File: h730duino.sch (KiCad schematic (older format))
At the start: 71 parts, among them J4 105162-0001, P1 Digital, P10 CONN_01X01, P11 CONN_01X01, P13 CONN_01X01, P2 Power, P3 Analog, P4 Analog, P5 PWM, P6 PWM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

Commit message: Replace non stocked components.
 - Redesign 5V/3.3V using TPS6216xDSGT
 - Use bigger crystal (move to 5031 case)
 - Change some components parts

Signed-off-by: Martin Ribelotta <martinribelotta@gmail.com>
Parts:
- removed C18, C22: 100n, Capacitor_SMD:C_0603_1608Metric, symbol Device:C_Small
- removed C20, C24: 2.2u, Capacitor_SMD:C_0603_1608Metric, symbol Device:C_Small
- removed U3: AP63203WU, Package_TO_SOT_SMD:TSOT-23-6, symbol Regulator_Switching:AP63203WU
- removed U4: AP63205WU, Package_TO_SOT_SMD:TSOT-23-6, symbol Regulator_Switching:AP63205WU
- added U3: TPS62162DSG, Package_SON:WSON-8-1EP_2x2mm_P0.5mm_EP0.9x1.6mm_ThermalVias, symbol Regulator_Switching:TPS62162DSG
- added U4: TPS62163DSG, Package_SON:WSON-8-1EP_2x2mm_P0.5mm_EP0.9x1.6mm_ThermalVias, symbol Regulator_Switching:TPS62163DSG
- C1: DESCRIPTION (none) -> Capacitor 4.7u 0603
- C10, C12: DESCRIPTION (none) -> Capacitor 20p 0603
- C11, C8, C9: DESCRIPTION (none) -> Capacitor 10p 0603
- C13: DESCRIPTION (none) -> Capacitor 1u 0603
- C14, C15, C16, C2, C3, C39, C4, C40, C41, C43, C44, C45, C46, C47, C48, C5, C6, C7: DESCRIPTION (none) -> Capacitor 100n 0603
- C17, C21: DESCRIPTION (none) -> Capacitor 10u 0603
- C19, C23: value 2.2u -> 22u; DESCRIPTION (none) -> Capacitor 2.2u 0603
- C42: DESCRIPTION (none) -> Capacitor 2.2u 0603
- D3, D4: DESCRIPTION (none) -> Led SMD 0603 red
- L1, L2: DESCRIPTION (none) -> ferrite bead 0603
- L3, L4: value 4.7u -> NR3015T2R2M; footprint Inductor_SMD:L_1210_3225Metric -> Inductor_SMD:L_Taiyo-Yuden_MD-3030; DESCRIPTION (none) -> Inductor 4.7uH 1210
- R26, R4, R5: DESCRIPTION (none) -> Resistor 1.5K 0603
- U1: DESCRIPTION (none) -> STM32H730ZBT6
- U10: DESCRIPTION (none) -> APS6404L-3SQN
- U12: DESCRIPTION (none) -> AP22814BW5
- U2: DESCRIPTION (none) -> W25Q32JVSS
- U5, U6, U8: DESCRIPTION (none) -> MAX40200AUK
- Y1: DESCRIPTION (none) -> Crystal 32.768KHz 3215
- Y2: footprint footprints:Crystal_SMD_3215-2Pin_3.2x1.5mm -> Crystal:Crystal_SMD_5032-2Pin_5.0x3.2mm; DESCRIPTION (none) -> Crystal 8MHz 3215
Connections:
- wire segments 265 -> 267
- no-connect marks 9 -> 11
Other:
- moved on the sheet: C17, C19, C21, C23, D3, D4, L4, R26, R4

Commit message: Fix in design:
 - Add r-series to QSPI interfaces
 - Change vCAP from 100n to 2.2u
 - Add pullup to SWCK/DIO and nRST
 - Remove AGND/DGND separation

Signed-off-by: Martin Ribelotta <martinribelotta@gmail.com>
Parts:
- removed L2: ferrite, Inductor_SMD:L_0603_1608Metric, symbol Device:L_Small
- added R20: 10K, Resistor_SMD:R_0603_1608Metric, symbol Device:R_Small
- added RN1: 0Rx5, Resistor_SMD:R_Array_Convex_5x0603, symbol Device:R_Pack05
- C14, C15: value 100n -> 2.2u
- R5: value 1K5 -> 10K
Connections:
- net labels removed: GNDA
- wire segments 267 -> 269
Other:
- moved on the sheet: SW1
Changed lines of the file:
@@
 L power:GND #PWR017
 U 1 1 602274CF
-P 850 2550
-F 0 "#PWR017" H 850 2300 50  0001 C CNN
-F 1 "GND" V 855 2422 50  0000 R CNN
-F 2 "" H 850 2550 50  0000 C CNN
-F 3 "" H 850 2550 50  0000 C CNN
-	1    850  2550
+P 800 2600
+F 0 "#PWR017" H 800 2350 50  0001 C CNN
+F 1 "GND" V 805 2472 50  0000 R CNN
+F 2 "" H 800 2600 50  0000 C CNN
+F 3 "" H 800 2600 50  0000 C CNN
+	1    800  2600
 	0    1    1    0
 $EndComp
@@
 P 3600 2850
 F 0 "C15" H 3508 2896 50  0000 R CNN
-F 1 "100n" H 3508 2805 50  0000 R CNN
+F 1 "2.2u" H 3508 2805 50  0000 R CNN
 F 2 "Capacitor_SMD:C_0603_1608Metric" H 3600 2850 50  0001 C CNN
 F 3 "~" H 3600 2850 50  0001 C CNN
@@
 P 4000 2850
 F 0 "C14" H 3908 2896 50  0000 R CNN
-F 1 "100n" H 3908 2805 50  0000 R CNN
+F 1 "2.2u" H 3908 2805 50  0000 R CNN
 F 2 "Capacitor_SMD:C_0603_1608Metric" H 4000 2850 50  0001 C CNN
 F 3 "~" H 4000 2850 50  0001 C CNN
@@
 L Switch:SW_Push SW1
 U 1 1 609B261A
-P 1050 2550
-F 0 "SW1" H 1050 2457 50  0000 C CNN
-F 1 "RESET" H 1050 2366 50  0000 C CNN
-F 2 "Button_Switch_THT:SW_Tactile_SPST_Angled_PTS645Vx39-2LFS" H 1050 2750 50  0001 C CNN
-F 3 "~" H 1050 2750 50  0001 C CNN
-	1    1050 2550
+P 1000 2600
+F 0 "SW1" H 1000 2507 50  0000 C CNN
+F 1 "RESET" H 1000 2416 50  0000 C CNN
+F 2 "Button_Switch_THT:SW_Tactile_SPST_Angled_PTS645Vx39-2LFS" H 1000 2800 50  0001 C CNN
+F 3 "~" H 1000 2800 50  0001 C CNN
+	1    1000 2600
 	1    0    0    -1
 $EndComp
@@
 P 850 2100
 F 0 "R5" H 792 2054 50  0000 R CNN
-F 1 "1K5" H 792 2145 50  0000 R CNN
+F 1 "10K" H 792 2145 50  0000 R CNN
 F 2 "Resistor_SMD:R_0603_1608Metric" H 850 2100 50  0001 C CNN
 F 3 "~" H 850 2100 50  0001 C CNN
@@
 	1    0    0    -1
 $EndComp
-Wire Wire Line
-	900  3750 1150 3750
-$Comp
-L Device:L_Small L2
-U 1 1 601A7F71
-P 800 3750
-F 0 "L2" V 711 3750 50  0000 C CNN
-F 1 "ferrite" V 620 3750 50  0000 C CNN
-F 2 "Inductor_SMD:L_0603_1608Metric" H 800 3750 50  0001 C CNN
-F 3 "~" H 800 3750 50  0001 C CNN
-F 4 "ferrite bead 0603" H 800 3750 50  0001 C CNN "DESCRIPTION"
-	1    800  3750
-	0    -1   -1   0
-$EndComp
 Connection ~ 1150 3750
-$Comp
-L power:GNDA #PWR014
-U 1 1 601A26C1
-P 1150 3750
-F 0 "#PWR014" H 1150 3500 50  0001 C CNN
-F 1 "GNDA" H 1155 3577 50  0000 C CNN
-F 2 "" H 1150 3750 50  0001 C CNN
-F 3 "" H 1150 3750 50  0001 C CNN
-	1    1150 3750
-	1    0    0    -1
-$EndComp
 Wire Wire Line
 	1150 3550 900  3550
@@
 Wire Wire Line
 	650  3550 700  3550
-Wire Wire Line
-	700  3750 650  3750
 $Comp
 L power:GND #PWR0110
@@
 Wire Wire Line
 	950  2000 1800 2000
-Text Label 1400 2550 0    50   ~ 0
+Text Label 1250 2600 0    50   ~ 0
 ~RST
-Wire Wire Line
-	1400 2550 1250 2550
 $Comp
 L stm32h730zbtx:STM32H730ZBT6 U1
@@
 Text Label 5300 2150 2    50   ~ 0
 USR_LED
-Text Label 5300 2750 2    50   ~ 0
+Text Label 4750 2750 2    50   ~ 0
 OCTOSPIM_P2_CLK
 Text Label 7700 3800 0    50   ~ 0
@@
 Connection ~ 1500 3550
 Wire Wire Line
-	650  3750 650  3950
-Wire Wire Line
 	650  3550 650  3300
 $Comp
 L power:GND #PWR0113
 U 1 1 60346253
-P 650 3950
-F 0 "#PWR0113" H 650 3700 50  0001 C CNN
-F 1 "GND" H 655 3777 50  0000 C CNN
-F 2 "" H 650 3950 50  0000 C CNN
-F 3 "" H 650 3950 50  0000 C CNN
-	1    650  3950
+P 1150 3750
+F 0 "#PWR0113" H 1150 3500 50  0001 C CNN
+F 1 "GND" H 1155 3577 50  0000 C CNN
+F 2 "" H 1150 3750 50  0000 C CNN
+F 3 "" H 1150 3750 50  0000 C CNN
+	1    1150 3750
 	1    0    0    -1
 $EndComp
@@
 	1    0    0    -1
 $EndComp
-Text Label 5300 2350 2    50   ~ 0
+Text Label 4750 2350 2    50   ~ 0
 OCTOSPIM_P2_IO0
-Text Label 5300 2450 2    50   ~ 0
+Text Label 4750 2450 2    50   ~ 0
 OCTOSPIM_P2_IO1
-Text Label 5300 2550 2    50   ~ 0
+Text Label 4750 2550 2    50   ~ 0
 OCTOSPIM_P2_IO2
-Text Label 5300 2650 2    50   ~ 0
+Text Label 4750 2650 2    50   ~ 0
 OCTOSPIM_P2_IO3
 Text Label 10400 6600 0    50   ~ 0
@@
 	10950 2200 10850 2200
 Connection ~ 10850 2200
+$Comp
+L Device:R_Small R20
+U 1 1 605BF408
+P 1500 2600
+F 0 "R20" V 1304 2600 50  0000 C CNN
+F 1 "10K" V 1395 2600 50  0000 C CNN
+F 2 "Resistor_SMD:R_0603_1608Metric" H 1500 2600 50  0001 C CNN
+F 3 "~" H 1500 2600 50  0001 C CNN
+F 4 "Resistor 1.5K 0603" H 1500 2600 50  0001 C CNN "DESCRIPTION"
+	1    1500 2600
+	0    -1   1    0
+$EndComp
+$Comp
+L power:+3V3 #PWR014
+U 1 1 605C04C4
+P 1600 2600
+F 0 "#PWR014" H 1600 2450 50  0001 C CNN
+F 1 "+3.3V" V 1615 2728 50  0000 L CNN
+F 2 "" H 1600 2600 50  0000 C CNN
+F 3 "" H 1600 2600 50  0000 C CNN
+	1    1600 2600
+	0    1    1    0
+$EndComp
+Wire Wire Line
+	1200 2600 1400 2600
+$Comp
+L Device:R_Pack05 RN1
+U 1 1 60649F7B
+P 4950 2550
+F 0 "RN1" V 5283 2550 50  0000 C CNN
+F 1 "0Rx5" V 5374 2550 50  0000 C CNN
+F 2 "Resistor_SMD:R_Array_Convex_5x0603" V 5325 2550 50  0001 C CNN
+F 3 "~" H 4950 2550 50  0001 C CNN
+	1    4950 2550
+	0    1    1    0
+$EndComp
+Wire Wire Line
+	5150 2350 5300 2350
+Wire Wire Line
+	5300 2450 5150 2450
+Wire Wire Line
+	5150 2550 5300 2550
+Wire Wire Line
+	5300 2650 5150 2650
+Wire Wire Line
+	5150 2750 5300 2750
 $EndSCHEMATC

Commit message: Major rework:
 - Split flash/ram in two QSPI iface
   - Flash is connected to QSPI2
   - PSRAM is connected to QSPI1
 - Move QSPI PSRAM near to P1
 - Reorder pins to P1 and P5
 - Reasign I2C5, UART4 to more convenient place
 - Reasign PWM pins to more convenient place
 - Rerarrange 25MHz ETHPHY crystal

Signed-off-by: Martin Ribelotta <martinribelotta@gmail.com>
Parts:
- removed P9: EXT, Socket_Arduino_Mega:Socket_Strip_Arduino_1x10, symbol Connector_Generic:Conn_01x10
- removed RN1: 0Rx5, Resistor_SMD:R_Array_Convex_5x0603, symbol Device:R_Pack05
- added J7: Conn_02x03_Odd_Even, Connector_PinHeader_2.54mm:PinHeader_2x03_P2.54mm_Vertical, symbol Connector_Generic:Conn_02x03_Odd_Even
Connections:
- net labels added: OCTOSPIM_P1_CLK, OCTOSPIM_P1_IO4, OCTOSPIM_P1_IO5, OCTOSPIM_P1_IO6, OCTOSPIM_P1_IO7
- net labels removed: EXT5, EXT6, EXT7, EXT8, EXT9
- wire segments 269 -> 267
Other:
- moved on the sheet: C41, D3, D4, R26, R4

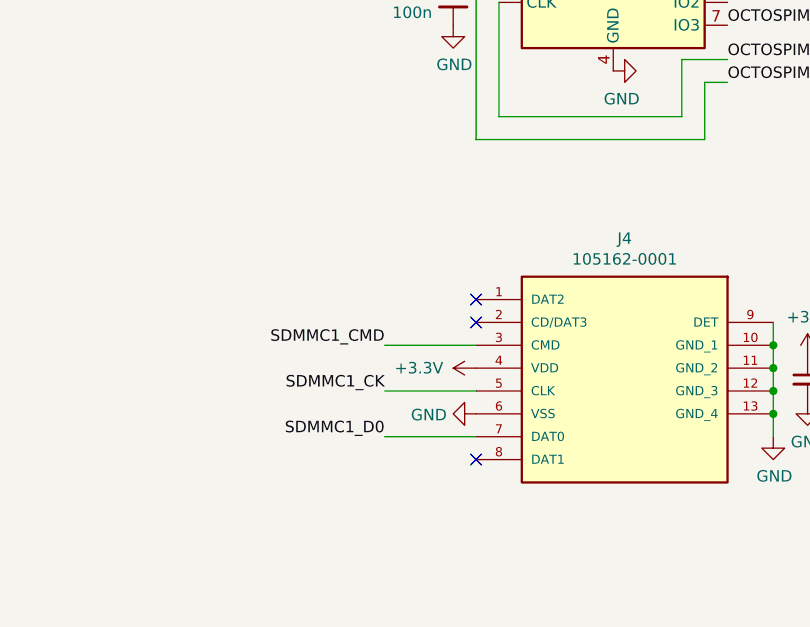
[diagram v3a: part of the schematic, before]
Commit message: Improve previous changes:
 - Add pullup resistors to uSD card slot
 - Reroute some signals for more space
 - Check impedance of QSPI/USB signals
 - Match length of uSD signals

Signed-off-by: Martin Ribelotta <martinribelotta@gmail.com>
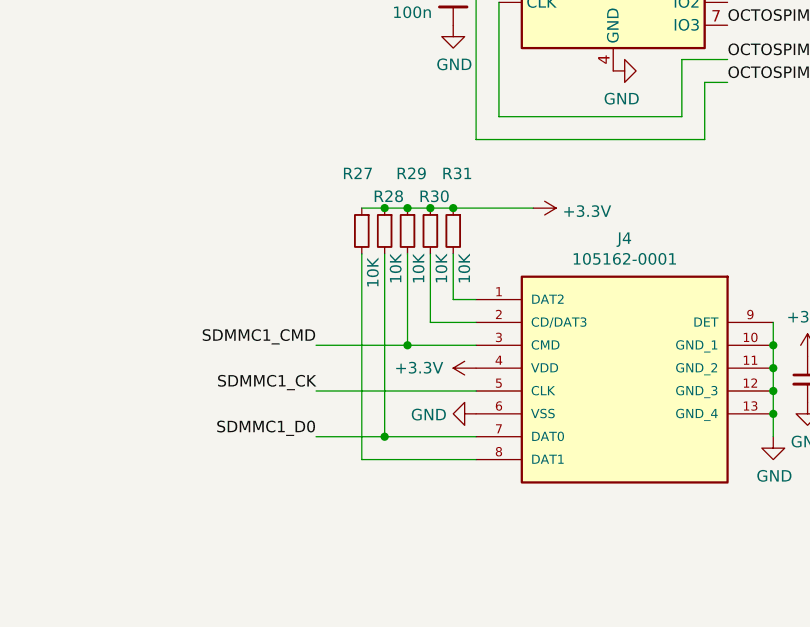
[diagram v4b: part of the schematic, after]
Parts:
- added R27, R28, R29, R30, R31: 10K, Resistor_SMD:R_0603_1608Metric, symbol Device:R_Small
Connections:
- net +3V3: now also R27.1, R28.1, R29.1, R30.1, R31.1
- net SDMMC1_CMD: now also R29.2
- net SDMMC1_D0: now also R28.2
- net at J4.1 (DAT2): now also R31.2
- net at J4.2 (CD/DAT3): now also R30.2
- net at J4.8 (DAT1): now also R27.2
- no-connect marks 11 -> 8
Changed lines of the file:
@@
 	1    0    0    -1
 $EndComp
-Text Label 6350 8200 2    50   ~ 0
+Text Label 6050 8200 2    50   ~ 0
 SDMMC1_D0
-Text Label 6350 8000 2    50   ~ 0
+Text Label 6050 8000 2    50   ~ 0
 SDMMC1_CK
-Text Label 6350 7800 2    50   ~ 0
+Text Label 6050 7800 2    50   ~ 0
 SDMMC1_CMD
 $Comp
@@
 	0    1    1    0
 $EndComp
-NoConn ~ 6750 8300
-NoConn ~ 6750 7700
-NoConn ~ 6750 7600
 $Comp
 L Device:C_Small C41
@@
 47
 Wire Wire Line
-	6350 7800 6750 7800
-Wire Wire Line
-	6350 8000 6750 8000
-Wire Wire Line
-	6350 8200 6750 8200
+	6050 8000 6750 8000
 $Comp
 L Connector_Generic:Conn_02x03_Odd_Even J7
@@
 	0    1    1    0
 $EndComp
+Wire Wire Line
+	6050 7800 6450 7800
+Wire Wire Line
+	6050 8200 6350 8200
+$Comp
+L Device:R_Small R31
+U 1 1 6069A575
+P 6650 7300
+F 0 "R31" H 6700 7550 50  0000 R CNN
+F 1 "10K" V 6600 7200 50  0000 R CNN
+F 2 "Resistor_SMD:R_0603_1608Metric" H 6650 7300 50  0001 C CNN
+F 3 "~" H 6650 7300 50  0001 C CNN
+F 4 "Resistor 1.5K 0603" H 6650 7300 50  0001 C CNN "DESCRIPTION"
+	1    6650 7300
+	-1   0    0    -1
+$EndComp
+$Comp
+L Device:R_Small R30
+U 1 1 6069CA86
+P 6550 7300
+F 0 "R30" H 6600 7450 50  0000 R CNN
+F 1 "10K" V 6500 7200 50  0000 R CNN
+F 2 "Resistor_SMD:R_0603_1608Metric" H 6550 7300 50  0001 C CNN
+F 3 "~" H 6550 7300 50  0001 C CNN
+F 4 "Resistor 1.5K 0603" H 6550 7300 50  0001 C CNN "DESCRIPTION"
+	1    6550 7300
+	-1   0    0    -1
+$EndComp
+$Comp
+L Device:R_Small R29
+U 1 1 6069CCE5
+P 6450 7300
+F 0 "R29" H 6500 7550 50  0000 R CNN
+F 1 "10K" V 6400 7200 50  0000 R CNN
+F 2 "Resistor_SMD:R_0603_1608Metric" H 6450 7300 50  0001 C CNN
+F 3 "~" H 6450 7300 50  0001 C CNN
+F 4 "Resistor 1.5K 0603" H 6450 7300 50  0001 C CNN "DESCRIPTION"
+	1    6450 7300
+	-1   0    0    -1
+$EndComp
+$Comp
+L Device:R_Small R28
+U 1 1 6069D01E
+P 6350 7300
+F 0 "R28" H 6400 7450 50  0000 R CNN
+F 1 "10K" V 6300 7200 50  0000 R CNN
+F 2 "Resistor_SMD:R_0603_1608Metric" H 6350 7300 50  0001 C CNN
+F 3 "~" H 6350 7300 50  0001 C CNN
+F 4 "Resistor 1.5K 0603" H 6350 7300 50  0001 C CNN "DESCRIPTION"
+	1    6350 7300
+	-1   0    0    -1
+$EndComp
+$Comp
+L Device:R_Small R27
+U 1 1 6069D327
+P 6250 7300
+F 0 "R27" H 6200 7550 50  0000 L CNN
+F 1 "10K" V 6200 7050 50  0000 L CNN
+F 2 "Resistor_SMD:R_0603_1608Metric" H 6250 7300 50  0001 C CNN
+F 3 "~" H 6250 7300 50  0001 C CNN
+F 4 "Resistor 1.5K 0603" H 6250 7300 50  0001 C CNN "DESCRIPTION"
+	1    6250 7300
+	-1   0    0    -1
+$EndComp
+Wire Wire Line
+	6650 7400 6650 7600
+Wire Wire Line
+	6650 7600 6750 7600
+Wire Wire Line
+	6750 7700 6550 7700
+Wire Wire Line
+	6550 7700 6550 7400
+Wire Wire Line
+	6450 7400 6450 7800
+Connection ~ 6450 7800
+Wire Wire Line
+	6450 7800 6750 7800
+Wire Wire Line
+	6350 7400 6350 8200
+Connection ~ 6350 8200
+Wire Wire Line
+	6350 8200 6750 8200
+Wire Wire Line
+	6250 7400 6250 8300
+Wire Wire Line
+	6250 8300 6750 8300
+Wire Wire Line
+	6250 7200 6350 7200
+Connection ~ 6350 7200
+Wire Wire Line
+	6350 7200 6450 7200
+Connection ~ 6450 7200
+Wire Wire Line
+	6450 7200 6550 7200
+Connection ~ 6550 7200
+Wire Wire Line
+	6550 7200 6650 7200
+Connection ~ 6650 7200
+Wire Wire Line
+	6650 7200 7000 7200
+$Comp
+L power:+3V3 #PWR062
+U 1 1 6073696E
+P 7000 7200
+F 0 "#PWR062" H 7000 7050 50  0001 C CNN
+F 1 "+3.3V" V 7015 7328 50  0000 L CNN
+F 2 "" H 7000 7200 50  0000 C CNN
+F 3 "" H 7000 7200 50  0000 C CNN
+	1    7000 7200
+	0    1    1    0
+$EndComp
